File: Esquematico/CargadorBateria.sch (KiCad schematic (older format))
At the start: 34 parts, among them IC1 BQ24070RHLR, J10 Conn_01x02_Female, J8 Conn_01x02_Male, J9 Barrel_Jack_Switch, U5 MT3608, U6 AMS1117-3.3

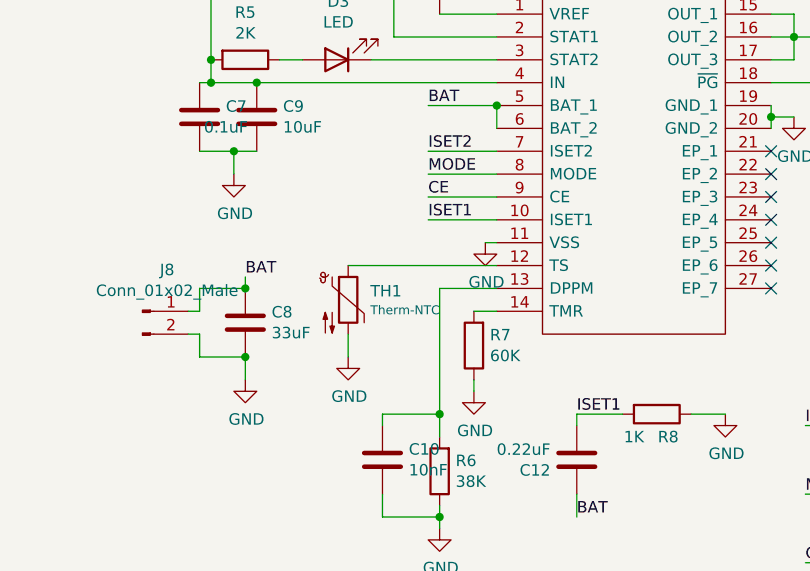
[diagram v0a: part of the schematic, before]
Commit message: cambios termistor
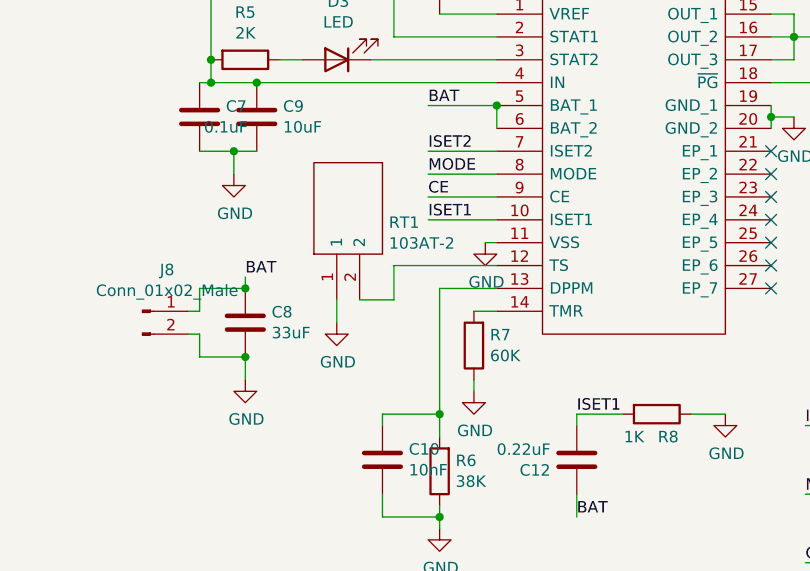
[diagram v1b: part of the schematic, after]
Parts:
- removed TH1: Therm-NTC, symbol Device:Thermistor_NTC
- added RT1: 103AT-2, 103AT2, symbol 103AT-2:103AT-2
- C10, C11, C12, C13, C14, C15, C7, C8, C9: footprint (none) -> Capacitor_SMD:C_0805_2012Metric_Pad1.18x1.45mm_HandSolder
- D2, D3, D4: footprint (none) -> LED_SMD:LED_0805_2012Metric_Pad1.15x1.40mm_HandSolder
- R10, R11, R12, R13, R14, R4, R5, R6, R7, R8, R9: footprint (none) -> Resistor_SMD:R_0805_2012Metric_Pad1.20x1.40mm_HandSolder
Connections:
- net GND: now also RT1.1
- net at IC1.12 (TS): now also RT1.2
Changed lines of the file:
@@
 F 0 "C11" H 4615 1246 50  0000 L CNN
 F 1 "0.1uF" H 4615 1155 50  0000 L CNN
-F 2 "" H 4538 1050 50  0001 C CNN
+F 2 "Capacitor_SMD:C_0805_2012Metric_Pad1.18x1.45mm_HandSolder" H 4538 1050 50  0001 C CNN
 F 3 "~" H 4500 1200 50  0001 C CNN
 	1    4500 1200
@@
 F 0 "C9" H 3815 1846 50  0000 L CNN
 F 1 "10uF" H 3815 1755 50  0000 L CNN
-F 2 "" H 3738 1650 50  0001 C CNN
+F 2 "Capacitor_SMD:C_0805_2012Metric_Pad1.18x1.45mm_HandSolder" H 3738 1650 50  0001 C CNN
 F 3 "~" H 3700 1800 50  0001 C CNN
 	1    3700 1800
@@
 F 0 "C8" H 3765 2746 50  0000 L CNN
 F 1 "33uF" H 3765 2655 50  0000 L CNN
-F 2 "" H 3688 2550 50  0001 C CNN
+F 2 "Capacitor_SMD:C_0805_2012Metric_Pad1.18x1.45mm_HandSolder" H 3688 2550 50  0001 C CNN
 F 3 "~" H 3650 2700 50  0001 C CNN
 	1    3650 2700
-	1    0    0    -1
-$EndComp
-$Comp
-L Device:Thermistor_NTC TH1
-U 1 1 61BA5AF2
-P 4100 2600
-F 0 "TH1" H 4197 2638 50  0000 L CNN
-F 1 "Therm-NTC" H 4197 2555 39  0000 L CNN
-F 2 "" H 4100 2650 50  0001 C CNN
-F 3 "~" H 4100 2650 50  0001 C CNN
-	1    4100 2600
 	1    0    0    -1
 $EndComp
@@
 F 0 "C15" H 10215 1796 50  0000 L CNN
 F 1 "22uF" H 10215 1705 50  0000 L CNN
-F 2 "" H 10138 1600 50  0001 C CNN
+F 2 "Capacitor_SMD:C_0805_2012Metric_Pad1.18x1.45mm_HandSolder" H 10138 1600 50  0001 C CNN
 F 3 "~" H 10100 1750 50  0001 C CNN
 	1    10100 1750
@@
 F 0 "R4" V 3443 1200 50  0000 C CNN
 F 1 "2K" V 3534 1200 50  0000 C CNN
-F 2 "" V 3580 1200 50  0001 C CNN
+F 2 "Resistor_SMD:R_0805_2012Metric_Pad1.20x1.40mm_HandSolder" V 3580 1200 50  0001 C CNN
 F 3 "~" H 3650 1200 50  0001 C CNN
 	1    3650 1200
@@
 F 0 "R5" V 3443 1550 50  0000 C CNN
 F 1 "2K" V 3534 1550 50  0000 C CNN
-F 2 "" V 3580 1550 50  0001 C CNN
+F 2 "Resistor_SMD:R_0805_2012Metric_Pad1.20x1.40mm_HandSolder" V 3580 1550 50  0001 C CNN
 F 3 "~" H 3650 1550 50  0001 C CNN
 	1    3650 1550
@@
 F 0 "D2" H 4043 945 50  0000 C CNN
 F 1 "LED" H 4043 1036 50  0000 C CNN
-F 2 "" H 4050 1200 50  0001 C CNN
+F 2 "LED_SMD:LED_0805_2012Metric_Pad1.15x1.40mm_HandSolder" H 4050 1200 50  0001 C CNN
 F 3 "~" H 4050 1200 50  0001 C CNN
 	1    4050 1200
@@
 F 0 "D3" H 4043 1295 50  0000 C CNN
 F 1 "LED" H 4043 1386 50  0000 C CNN
-F 2 "" H 4050 1550 50  0001 C CNN
+F 2 "LED_SMD:LED_0805_2012Metric_Pad1.15x1.40mm_HandSolder" H 4050 1550 50  0001 C CNN
 F 3 "~" H 4050 1550 50  0001 C CNN
 	1    4050 1550
@@
 F 0 "D4" H 6393 2017 50  0000 C CNN
 F 1 "LED" H 6393 1926 50  0000 C CNN
-F 2 "" H 6400 1800 50  0001 C CNN
+F 2 "LED_SMD:LED_0805_2012Metric_Pad1.15x1.40mm_HandSolder" H 6400 1800 50  0001 C CNN
 F 3 "~" H 6400 1800 50  0001 C CNN
 	1    6400 1800
@@
 F 0 "C13" H 6915 1696 50  0000 L CNN
 F 1 "0.1uF" H 6915 1605 50  0000 L CNN
-F 2 "" H 6838 1500 50  0001 C CNN
+F 2 "Capacitor_SMD:C_0805_2012Metric_Pad1.18x1.45mm_HandSolder" H 6838 1500 50  0001 C CNN
 F 3 "~" H 6800 1650 50  0001 C CNN
 	1    6800 1650
@@
 	1    0    0    -1
 $EndComp
-Wire Wire Line
-	4100 2450 4750 2450
 $Comp
 L Device:R R8
@@
 F 0 "R8" V 5550 3150 50  0000 C CNN
 F 1 "1K" V 5550 3000 50  0000 C CNN
-F 2 "" V 5380 3100 50  0001 C CNN
+F 2 "Resistor_SMD:R_0805_2012Metric_Pad1.20x1.40mm_HandSolder" V 5380 3100 50  0001 C CNN
 F 3 "~" H 5450 3100 50  0001 C CNN
 	1    5450 3100
@@
 F 0 "R7" H 4580 2754 50  0000 R CNN
 F 1 "60K" H 4580 2845 50  0000 R CNN
-F 2 "" V 4580 2800 50  0001 C CNN
+F 2 "Resistor_SMD:R_0805_2012Metric_Pad1.20x1.40mm_HandSolder" V 4580 2800 50  0001 C CNN
 F 3 "~" H 4650 2800 50  0001 C CNN
 	1    4650 2800
@@
 F 0 "C10" H 4365 3346 50  0000 L CNN
 F 1 "10nF" H 4365 3255 50  0000 L CNN
-F 2 "" H 4288 3150 50  0001 C CNN
+F 2 "Capacitor_SMD:C_0805_2012Metric_Pad1.18x1.45mm_HandSolder" H 4288 3150 50  0001 C CNN
 F 3 "~" H 4250 3300 50  0001 C CNN
 	1    4250 3300
@@
 F 0 "R6" H 4430 3304 50  0000 R CNN
 F 1 "38K" H 4430 3395 50  0000 R CNN
-F 2 "" V 4430 3350 50  0001 C CNN
+F 2 "Resistor_SMD:R_0805_2012Metric_Pad1.20x1.40mm_HandSolder" V 4430 3350 50  0001 C CNN
 F 3 "~" H 4500 3350 50  0001 C CNN
 	1    4500 3350
@@
 F 0 "R10" V 6393 3150 50  0000 C CNN
 F 1 "100K" V 6484 3150 50  0000 C CNN
-F 2 "" V 6530 3150 50  0001 C CNN
+F 2 "Resistor_SMD:R_0805_2012Metric_Pad1.20x1.40mm_HandSolder" V 6530 3150 50  0001 C CNN
 F 3 "~" H 6600 3150 50  0001 C CNN
 	1    6600 3150
@@
 F 0 "R11" V 6393 3450 50  0000 C CNN
 F 1 "100K" V 6484 3450 50  0000 C CNN
-F 2 "" V 6530 3450 50  0001 C CNN
+F 2 "Resistor_SMD:R_0805_2012Metric_Pad1.20x1.40mm_HandSolder" V 6530 3450 50  0001 C CNN
 F 3 "~" H 6600 3450 50  0001 C CNN
 	1    6600 3450
@@
 F 0 "R12" V 6393 3750 50  0000 C CNN
 F 1 "100K" V 6484 3750 50  0000 C CNN
-F 2 "" V 6530 3750 50  0001 C CNN
+F 2 "Resistor_SMD:R_0805_2012Metric_Pad1.20x1.40mm_HandSolder" V 6530 3750 50  0001 C CNN
 F 3 "~" H 6600 3750 50  0001 C CNN
 	1    6600 3750
@@
 F 0 "C14" H 7265 1696 50  0000 L CNN
 F 1 "22uF" H 7265 1605 50  0000 L CNN
-F 2 "" H 7188 1500 50  0001 C CNN
+F 2 "Capacitor_SMD:C_0805_2012Metric_Pad1.18x1.45mm_HandSolder" H 7188 1500 50  0001 C CNN
 F 3 "~" H 7150 1650 50  0001 C CNN
 	1    7150 1650
@@
 L power:GND #PWR0130
 U 1 1 61DBD0AF
-P 4100 2850
-F 0 "#PWR0130" H 4100 2600 50  0001 C CNN
-F 1 "GND" H 4105 2677 50  0000 C CNN
-F 2 "" H 4100 2850 50  0001 C CNN
-F 3 "" H 4100 2850 50  0001 C CNN
-	1    4100 2850
-	1    0    0    -1
-$EndComp
-Wire Wire Line
-	4100 2750 4100 2850
+P 4050 2700
+F 0 "#PWR0130" H 4050 2450 50  0001 C CNN
+F 1 "GND" H 4055 2527 50  0000 C CNN
+F 2 "" H 4050 2700 50  0001 C CNN
+F 3 "" H 4050 2700 50  0001 C CNN
+	1    4050 2700
+	1    0    0    -1
+$EndComp
 Wire Wire Line
 	4500 3200 4500 3100
@@
 F 0 "C7" H 3565 1846 50  0000 L CNN
 F 1 "0.1uF" H 3565 1755 50  0000 C CNN
-F 2 "" H 3488 1650 50  0001 C CNN
+F 2 "Capacitor_SMD:C_0805_2012Metric_Pad1.18x1.45mm_HandSolder" H 3488 1650 50  0001 C CNN
 F 3 "~" H 3450 1800 50  0001 C CNN
 	1    3450 1800
@@
 F 0 "C12" H 5215 3346 50  0000 L CNN
 F 1 "0.22uF" H 5215 3255 50  0000 L CNN
-F 2 "" H 5138 3150 50  0001 C CNN
+F 2 "Capacitor_SMD:C_0805_2012Metric_Pad1.18x1.45mm_HandSolder" H 5138 3150 50  0001 C CNN
 F 3 "~" H 5100 3300 50  0001 C CNN
 	1    5100 3300
@@
 F 0 "R9" V 6193 2200 50  0000 C CNN
 F 1 "2K" V 6284 2200 50  0000 C CNN
-F 2 "" V 6330 2200 50  0001 C CNN
+F 2 "Resistor_SMD:R_0805_2012Metric_Pad1.20x1.40mm_HandSolder" V 6330 2200 50  0001 C CNN
 F 3 "~" H 6400 2200 50  0001 C CNN
 	1    6400 2200
@@
 F 0 "R13" H 9530 1504 50  0000 R CNN
 F 1 "7.5K" H 9530 1595 50  0000 R CNN
-F 2 "" V 9530 1550 50  0001 C CNN
+F 2 "Resistor_SMD:R_0805_2012Metric_Pad1.20x1.40mm_HandSolder" V 9530 1550 50  0001 C CNN
 F 3 "~" H 9600 1550 50  0001 C CNN
 	1    9600 1550
@@
 F 0 "R14" H 9530 1954 50  0000 R CNN
 F 1 "1K" H 9530 2045 50  0000 R CNN
-F 2 "" V 9530 2000 50  0001 C CNN
+F 2 "Resistor_SMD:R_0805_2012Metric_Pad1.20x1.40mm_HandSolder" V 9530 2000 50  0001 C CNN
 F 3 "~" H 9600 2000 50  0001 C CNN
 	1    9600 2000
@@
 	3500 1200 3500 850
 Connection ~ 3500 1200
+$Comp
+L 103AT-2:103AT-2 RT1
+U 1 1 61E0D1F2
+P 4050 2600
+F 0 "RT1" V 4388 2372 50  0000 R CNN
+F 1 "103AT-2" V 4297 2372 50  0000 R CNN
+F 2 "103AT2" H 4700 2700 50  0001 L CNN
+F 3 "https://datasheet.datasheetarchive.com/originals/distributors/Datasheets-30/DSA-588185.pdf" H 4700 2600 50  0001 L CNN
+F 4 "NTC Thermistors 10kohm 1%" H 4700 2500 50  0001 L CNN "Description"
+F 5 "8" H 4700 2400 50  0001 L CNN "Height"
+F 6 "Semitec" H 4700 2300 50  0001 L CNN "Manufacturer_Name"
+F 7 "103AT-2" H 4700 2200 50  0001 L CNN "Manufacturer_Part_Number"
+F 8 "954-103AT-2" H 4700 2100 50  0001 L CNN "Mouser Part Number"
+F 9 "https://www.mouser.co.uk/ProductDetail/Semitec/103AT-2?qs=wgO0AD0o1vvcDzsKguD%252Bew%3D%3D" H 4700 2000 50  0001 L CNN "Mouser Price/Stock"
+F 10 "" H 4700 1900 50  0001 L CNN "Arrow Part Number"
+F 11 "" H 4700 1800 50  0001 L CNN "Arrow Price/Stock"
+	1    4050 2600
+	0    -1   -1   0
+$EndComp
+Wire Wire Line
+	4750 2450 4300 2450
+Wire Wire Line
+	4300 2450 4300 2600
+Wire Wire Line
+	4300 2600 4150 2600
+Wire Wire Line
+	4050 2700 4050 2600
 $EndSCHEMATC

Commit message: Carga elementos PCB
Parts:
- J10: footprint (none) -> Connector_PinSocket_2.54mm:PinSocket_1x02_P2.54mm_Vertical
- J8: footprint (none) -> Connector_PinHeader_2.54mm:PinHeader_1x02_P2.54mm_Vertical
- J9: footprint (none) -> Connector_BarrelJack:BarrelJack_CUI_PJ-102AH_Horizontal
- L1: footprint (none) -> Inductor_SMD:L_0805_2012Metric
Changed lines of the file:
@@
 F 0 "J8" H 3308 2831 50  0000 C CNN
 F 1 "Conn_01x02_Male" H 3308 2740 50  0000 C CNN
-F 2 "" H 3200 2650 50  0001 C CNN
+F 2 "Connector_PinHeader_2.54mm:PinHeader_1x02_P2.54mm_Vertical" H 3200 2650 50  0001 C CNN
 F 3 "~" H 3200 2650 50  0001 C CNN
 	1    3200 2650
@@
 F 0 "L1" V 8669 1150 50  0000 C CNN
 F 1 "22uH" V 8760 1150 50  0000 C CNN
-F 2 "" H 8850 1150 50  0001 C CNN
+F 2 "Inductor_SMD:L_0805_2012Metric" H 8850 1150 50  0001 C CNN
 F 3 "~" H 8850 1150 50  0001 C CNN
 	1    8850 1150
@@
 F 0 "J10" H 8492 3185 50  0000 C CNN
 F 1 "Conn_01x02_Female" H 8492 3094 50  0000 C CNN
-F 2 "" H 8600 3000 50  0001 C CNN
+F 2 "Connector_PinSocket_2.54mm:PinSocket_1x02_P2.54mm_Vertical" H 8600 3000 50  0001 C CNN
 F 3 "~" H 8600 3000 50  0001 C CNN
 	1    8600 3000
@@
 F 0 "J9" H 1657 1667 50  0000 C CNN
 F 1 "Barrel_Jack_Switch" H 1657 1576 50  0000 C CNN
-F 2 "" H 1650 1310 50  0001 C CNN
+F 2 "Connector_BarrelJack:BarrelJack_CUI_PJ-102AH_Horizontal" H 1650 1310 50  0001 C CNN
 F 3 "~" H 1650 1310 50  0001 C CNN
 	1    1600 1350

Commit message: footprints terminados
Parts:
- RT1: footprint 103AT2 -> Resistor_THT:R_Axial_DIN0204_L3.6mm_D1.6mm_P2.54mm_Vertical
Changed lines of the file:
@@
 F 0 "RT1" V 4388 2372 50  0000 R CNN
 F 1 "103AT-2" V 4297 2372 50  0000 R CNN
-F 2 "103AT2" H 4700 2700 50  0001 L CNN
+F 2 "Resistor_THT:R_Axial_DIN0204_L3.6mm_D1.6mm_P2.54mm_Vertical" H 4700 2700 50  0001 L CNN
 F 3 "https://datasheet.datasheetarchive.com/originals/distributors/Datasheets-30/DSA-588185.pdf" H 4700 2600 50  0001 L CNN
 F 4 "NTC Thermistors 10kohm 1%" H 4700 2500 50  0001 L CNN "Description"
